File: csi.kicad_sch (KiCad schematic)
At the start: 62 parts, among them J7 WE_68715014522, J8 WE_68715014522, U24 AP22653FDZ-7, U25 AP22653FDZ-7, U26 PCA9547BS, U27 AP22653FDZ-7, U28 AP22653FDZ-7, U31 NTS0102GT, U32 NTS0102GT

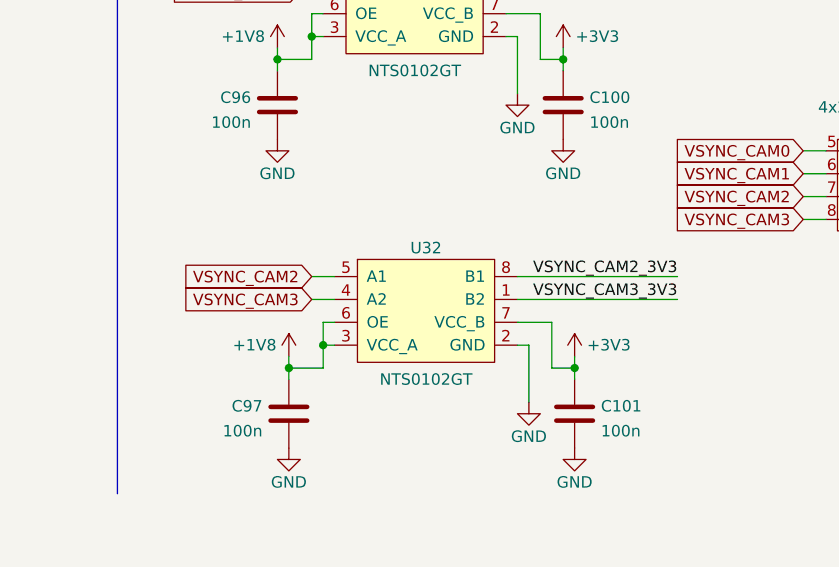
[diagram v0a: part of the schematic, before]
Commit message: Added exp conn resistors
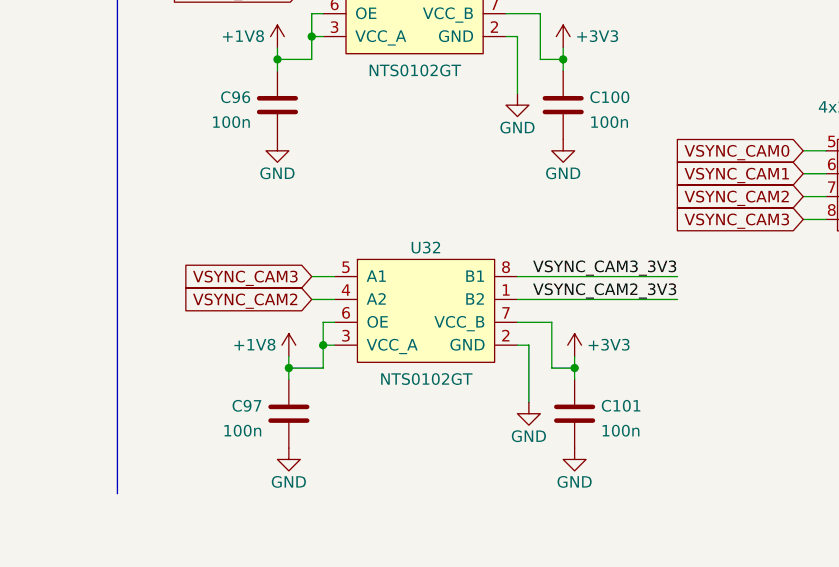
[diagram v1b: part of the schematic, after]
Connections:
- net VSYNC_CAM2: now also U32.4 (A2); no longer U32.5 (A1)
- net VSYNC_CAM2_3V3: now also U32.1 (B2); no longer U32.8 (B1)
- net VSYNC_CAM3: now also U32.5 (A1); no longer U32.4 (A2)
- net VSYNC_CAM3_3V3: now also U32.8 (B1); no longer U32.1 (B2)
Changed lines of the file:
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@@
     (effects (font (size 1.27 1.27)) (justify left bottom))
   )
-  (label "VSYNC_CAM3_3V3" (at 361.95 231.14 180)
+  (label "VSYNC_CAM3_3V3" (at 361.95 228.6 180)
     (effects (font (size 1.27 1.27)) (justify right bottom))
   )
@@
     (effects (font (size 1.27 1.27)) (justify left bottom))
   )
-  (label "VSYNC_CAM2_3V3" (at 361.95 228.6 180)
+  (label "VSYNC_CAM2_3V3" (at 361.95 231.14 180)
     (effects (font (size 1.27 1.27)) (justify right bottom))
   )
@@
     )
   )
-  (global_label "VSYNC_CAM2" (shape input) (at 321.31 228.6 180)
+  (global_label "VSYNC_CAM2" (shape input) (at 321.31 231.14 180)
     (effects (font (size 1.27 1.27)) (justify right))
-    (property "Intersheet References" "${INTERSHEET_REFS}" (id 0) (at 306.07 228.6 0)
+    (property "Intersheet References" "${INTERSHEET_REFS}" (id 0) (at 306.07 231.14 0)
       (effects (font (size 1.27 1.27)) (justify right))
     )
@@
     )
   )
-  (global_label "VSYNC_CAM3" (shape input) (at 321.31 231.14 180)
+  (global_label "VSYNC_CAM3" (shape input) (at 321.31 228.6 180)
     (effects (font (size 1.27 1.27)) (justify right))
-    (property "Intersheet References" "${INTERSHEET_REFS}" (id 0) (at 306.07 231.14 0)
+    (property "Intersheet References" "${INTERSHEET_REFS}" (id 0) (at 306.07 228.6 0)
       (effects (font (size 1.27 1.27)) (justify right))
     )

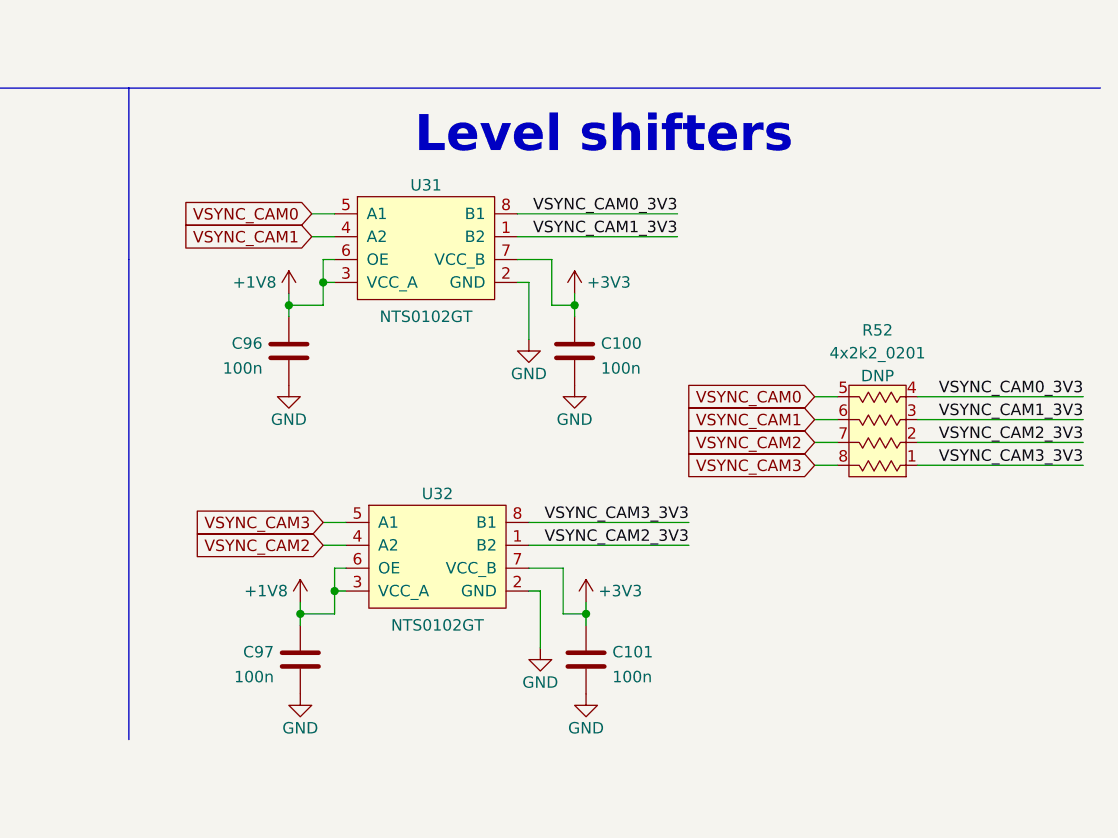
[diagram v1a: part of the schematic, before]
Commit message: Routed CSI vsync and M.2 low speed signals
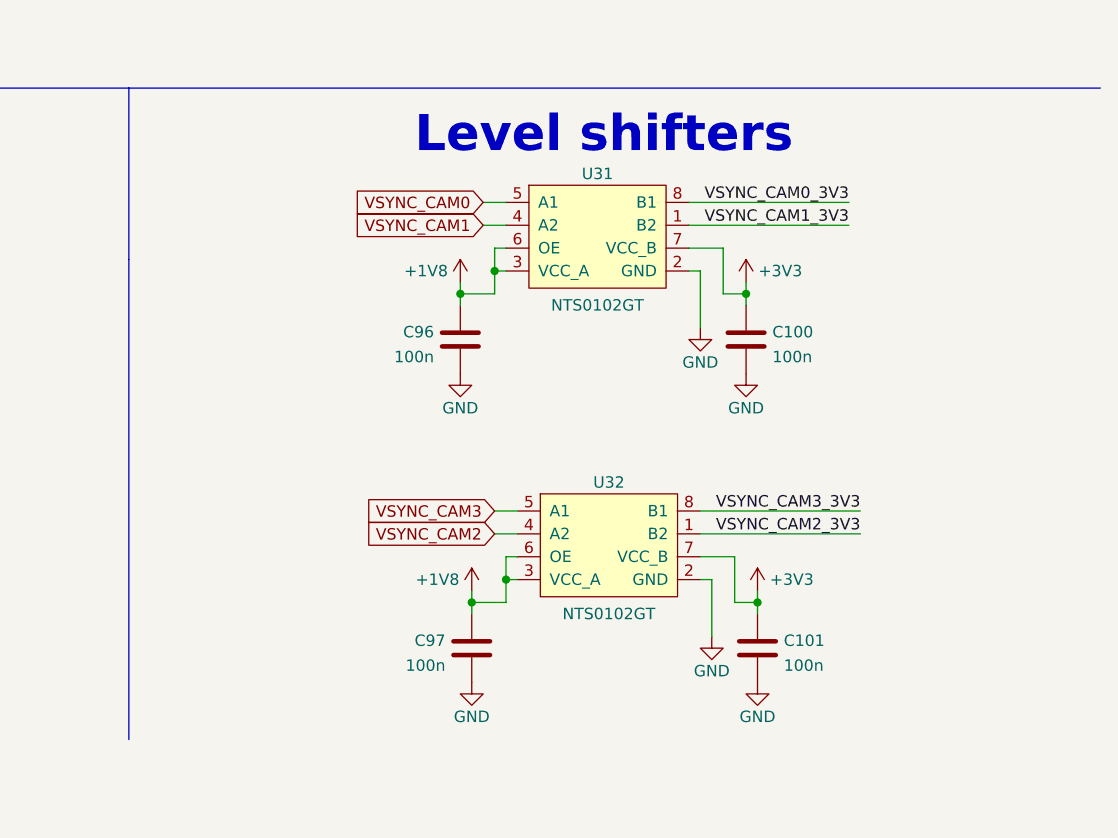
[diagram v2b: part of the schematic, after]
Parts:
- removed R52: 4x2k2_0201_array, antmicro-footprints:EXB18V, symbol antmicroResistorNetworksArrays:4x2k2_0201_array
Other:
- moved on the sheet: C100, C101, C96, C97, U31, U32

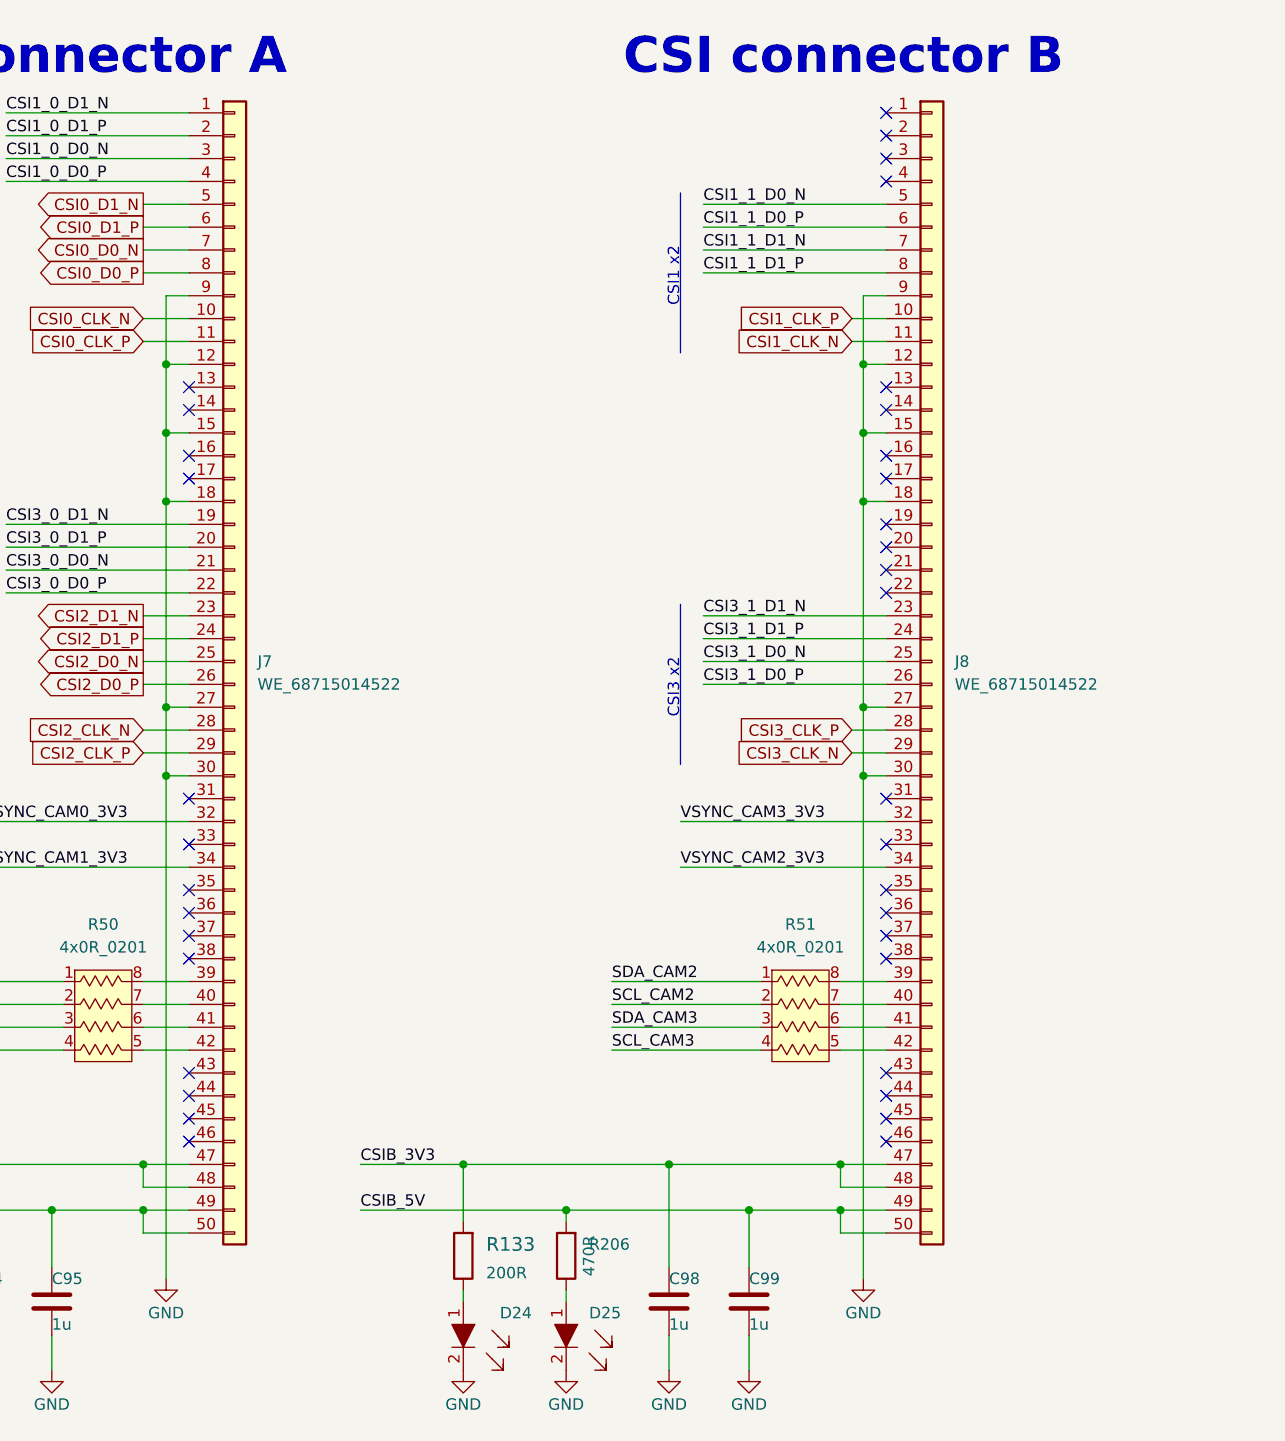
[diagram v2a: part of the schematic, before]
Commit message: Fixed DRC errors, fixed swapped SDA/SCL
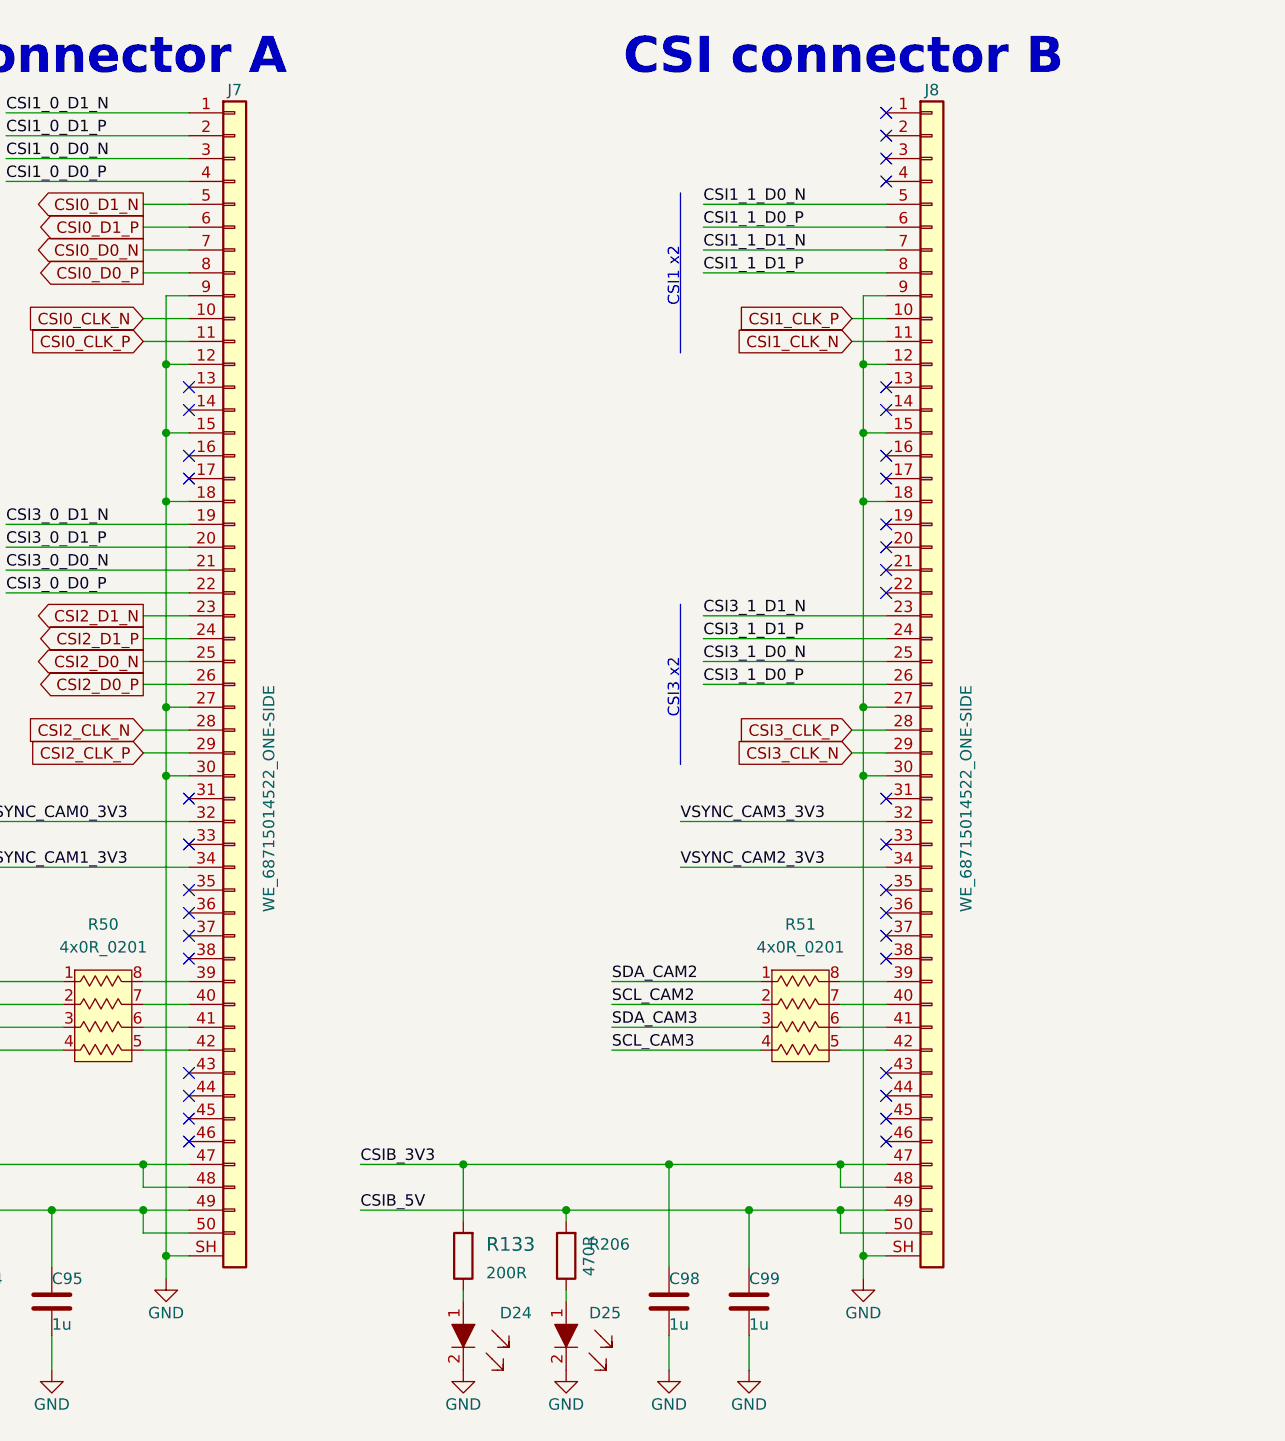
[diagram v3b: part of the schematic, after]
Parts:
- J7, J8: value WE_68715014522 -> WE_68715014522_ONE-SIDE; footprint antmicro-footprints:WE_68715014522 -> antmicro-footprints:WE_68715014522_ONE-SIDE; symbol antmicroFCCConnectors:WE_68715014522 -> antmicroFCCConnectors:WE_68715014522_ONE-SIDE
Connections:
- net GND: now also J7.SH (SHLD), J8.SH (SHLD)
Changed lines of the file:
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@@
   (junction (at 358.14 144.78) (diameter 0) (color 0 0 0 0)
   )
+  (junction (at 360.68 149.86) (diameter 0) (color 0 0 0 0)
+  )
   (junction (at 147.32 46.99) (diameter 0) (color 0 0 0 0)
   )
@@
   (junction (at 280.67 144.78) (diameter 0) (color 0 0 0 0)
   )
+  (junction (at 283.21 149.86) (diameter 0) (color 0 0 0 0)
+  )
   (junction (at 339.09 139.7) (diameter 0) (color 0 0 0 0)
   )
@@
     (stroke (width 0) (type default) (color 0 0 0 0))
   )
-  (wire (pts (xy 283.21 96.52) (xy 283.21 152.4))
+  (wire (pts (xy 283.21 96.52) (xy 283.21 149.86))
     (stroke (width 0) (type default) (color 0 0 0 0))
   )
@@
     (stroke (width 0) (type default) (color 0 0 0 0))
   )
+  (wire (pts (xy 283.21 149.86) (xy 283.21 152.4))
+    (stroke (width 0) (type default) (color 0 0 0 0))
+  )
   (wire (pts (xy 316.23 153.67) (xy 316.23 154.94))
     (stroke (width 0) (type default) (color 0 0 0 0))
@@
     (stroke (width 0) (type default) (color 0 0 0 0))
   )
+  (wire (pts (xy 360.68 149.86) (xy 363.22 149.86))
+    (stroke (width 0) (type default) (color 0 0 0 0))
+  )
   (wire (pts (xy 41.91 58.42) (xy 63.5 58.42))
     (stroke (width 0) (type default) (color 0 0 0 0))
@@
     (stroke (width 0) (type default) (color 0 0 0 0))
   )
+  (wire (pts (xy 360.68 149.86) (xy 360.68 152.4))
+    (stroke (width 0) (type default) (color 0 0 0 0))
+  )
   (wire (pts (xy 105.41 231.14) (xy 96.52 231.14))
     (stroke (width 0) (type default) (color 0 0 0 0))
@@
     (stroke (width 0) (type default) (color 0 0 0 0))
   )
-  (wire (pts (xy 360.68 96.52) (xy 360.68 152.4))
+  (wire (pts (xy 360.68 96.52) (xy 360.68 149.86))
     (stroke (width 0) (type default) (color 0 0 0 0))
   )
@@
     (stroke (width 0) (type default) (color 0 0 0 0))
   )
+  (wire (pts (xy 283.21 149.86) (xy 285.75 149.86))
+    (stroke (width 0) (type default) (color 0 0 0 0))
+  )
   (wire (pts (xy 166.37 39.37) (xy 186.69 39.37))
     (stroke (width 0) (type default) (color 0 0 0 0))
@@
     (pin "1")
   )
-  (symbol (lib_id "antmicroFCCConnectors:WE_68715014522") (at 368.3 63.5 0) (unit 1)
-    (in_bom yes) (on_board yes) (fields_autoplaced)
-    (property "Reference" "J8" (id 0) (at 370.84 83.8199 0)
-      (effects (font (size 1.27 1.27)) (justify left))
-    )
-    (property "Value" "WE_68715014522" (id 1) (at 370.84 86.3599 0)
-      (effects (font (size 1.27 1.27)) (justify left))
-    )
-    (property "Footprint" "antmicro-footprints:WE_68715014522" (id 2) (at 363.22 153.67 0)
+  (symbol (lib_id "antmicroFCCConnectors:WE_68715014522_ONE-SIDE") (at 368.3 63.5 0) (unit 1)
+    (in_bom yes) (on_board yes)
+    (property "Reference" "J8" (id 0) (at 368.3 20.32 0))
+    (property "Value" "WE_68715014522_ONE-SIDE" (id 1) (at 372.11 99.06 90))
+    (property "Footprint" "antmicro-footprints:WE_68715014522_ONE-SIDE" (id 2) (at 363.22 162.56 0)
       (effects (font (size 1.27 1.27)) hide)
     )
-    (property "Datasheet" "https://katalog.we-online.de/em/datasheet/6871xx14522.pdf" (id 3) (at 368.3 156.21 0)
+    (property "Datasheet" "" (id 3) (at 368.3 165.1 0)
       (effects (font (size 1.27 1.27)) hide)
     )
@@
     (pin "8")
     (pin "9")
+    (pin "SH")
   )
   (symbol (lib_id "antmicroLEDIndicationDiscrete:LTST-C190GKT") (at 250.19 160.02 270) (unit 1)
@@
     (pin "2")
   )
-  (symbol (lib_id "antmicroFCCConnectors:WE_68715014522") (at 290.83 63.5 0) (unit 1)
+  (symbol (lib_id "antmicroFCCConnectors:WE_68715014522_ONE-SIDE") (at 290.83 63.5 0) (unit 1)
     (in_bom yes) (on_board yes)
-    (property "Reference" "J7" (id 0) (at 293.37 83.8199 0)
-      (effects (font (size 1.27 1.27)) (justify left))
-    )
-    (property "Value" "WE_68715014522" (id 1) (at 293.37 86.3599 0)
-      (effects (font (size 1.27 1.27)) (justify left))
-    )
-    (property "Footprint" "antmicro-footprints:WE_68715014522" (id 2) (at 285.75 153.67 0)
+    (property "Reference" "J7" (id 0) (at 290.83 20.32 0))
+    (property "Value" "WE_68715014522_ONE-SIDE" (id 1) (at 294.64 99.06 90))
+    (property "Footprint" "antmicro-footprints:WE_68715014522_ONE-SIDE" (id 2) (at 285.75 162.56 0)
       (effects (font (size 1.27 1.27)) hide)
     )
-    (property "Datasheet" "https://katalog.we-online.de/em/datasheet/6871xx14522.pdf" (id 3) (at 290.83 156.21 0)
+    (property "Datasheet" "" (id 3) (at 290.83 165.1 0)
       (effects (font (size 1.27 1.27)) hide)
     )
@@
     (pin "8")
     (pin "9")
+    (pin "SH")
   )
   (symbol (lib_id "power:GND") (at 41.91 91.44 0) (unit 1)
